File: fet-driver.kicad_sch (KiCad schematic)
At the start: 32 parts, among them Q21 AO3401, Q22 AO3401, Q23 AO3401, Q24 AO3401, Q25 AO3401, Q26 AO3401, Q27 AO3401, Q28 AO3401

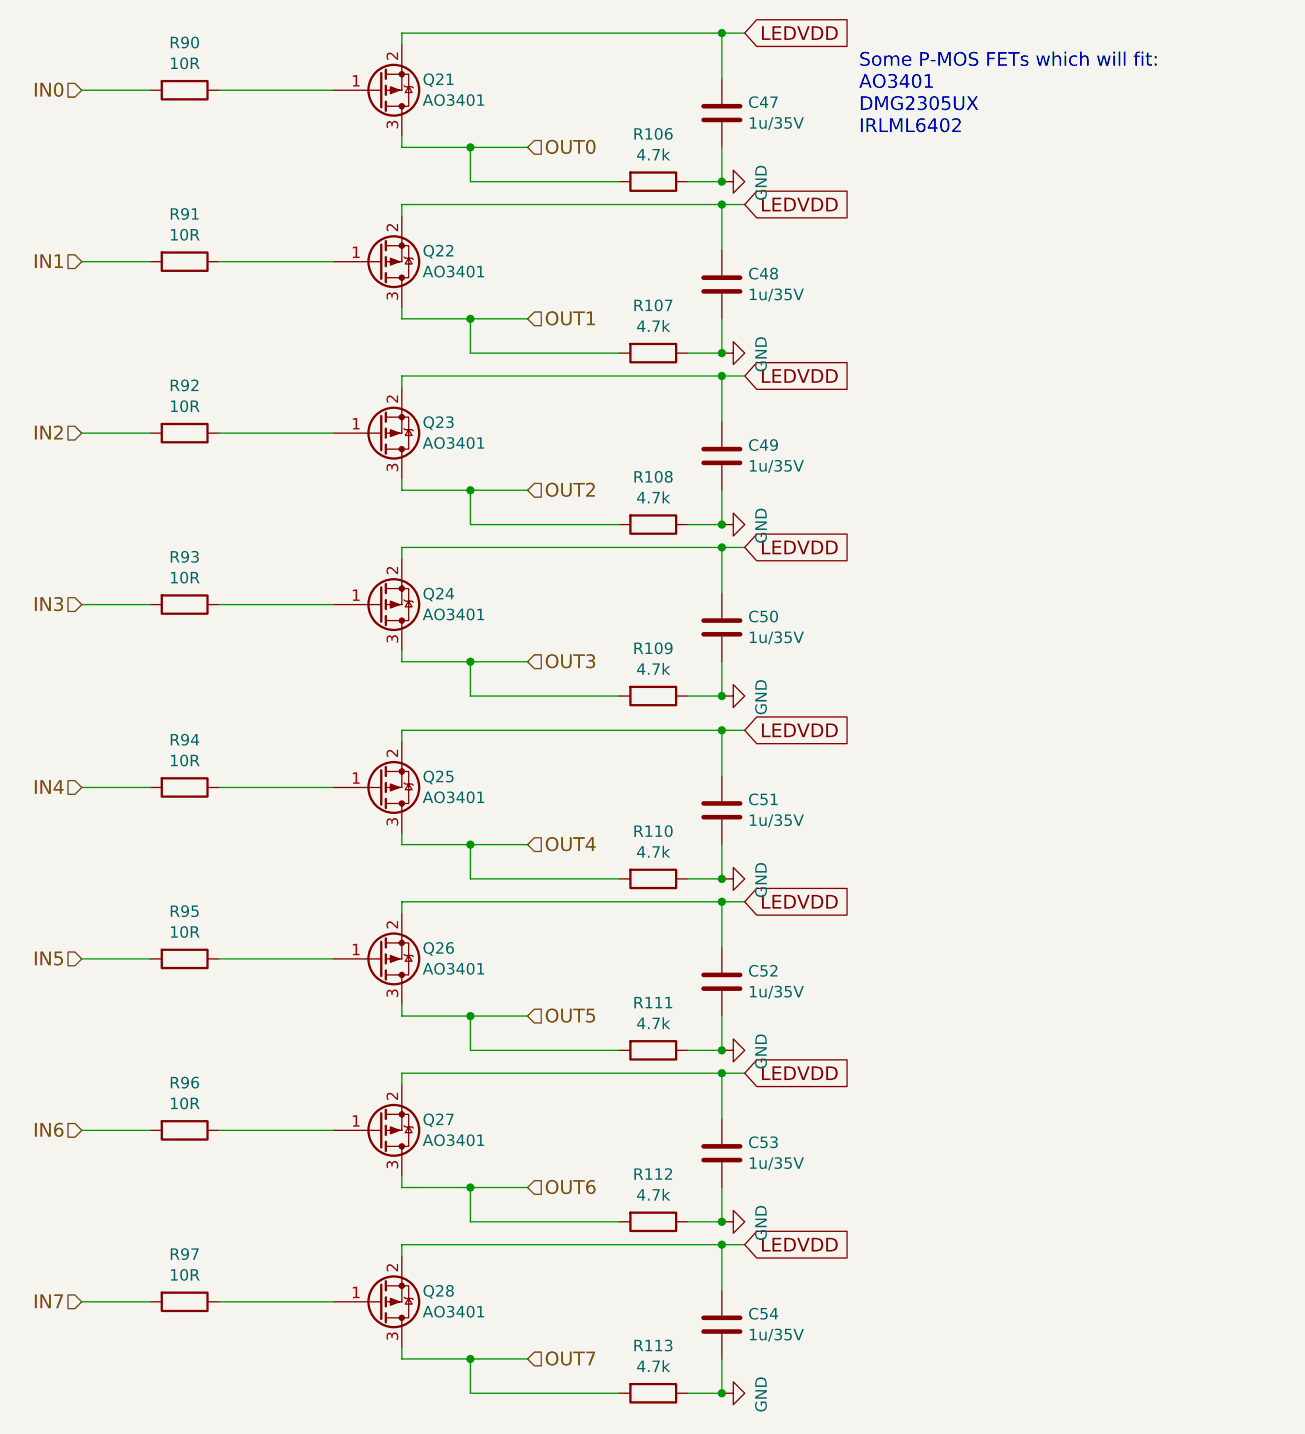
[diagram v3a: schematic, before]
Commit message: WROOM32 coupling capacitor order fixed; Added FB on long line to board left-most sensors
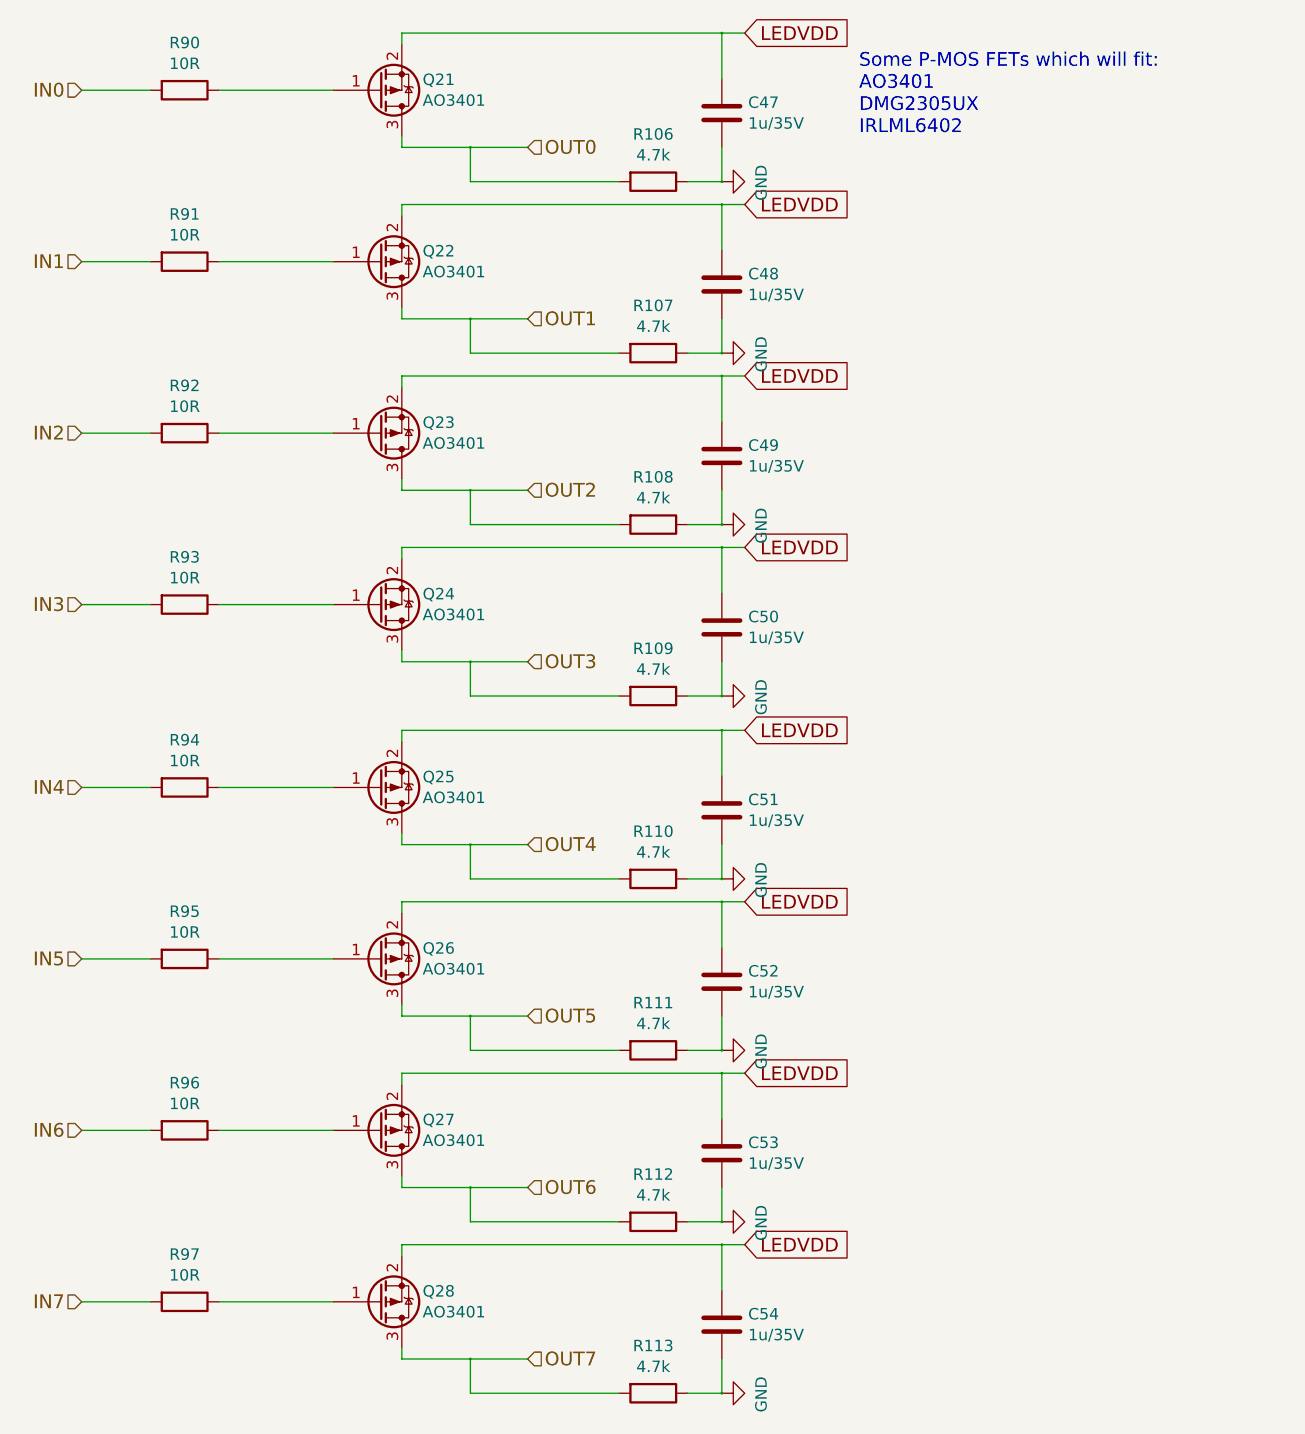
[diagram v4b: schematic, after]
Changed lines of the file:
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@@
-(kicad_sch (version 20200618) (host eeschema "5.99.0-unknown-7340c97~89~ubuntu18.04.1")
-  (page 1 10)
+(kicad_sch (version 20200714) (host eeschema "5.99.0-unknown-e5f2015a9~89~ubuntu18.04.1")
+  (page 0 10)
   (paper "A4")
-  (junction (at 119.38 39.37) (diameter 0) (color 0 0 0 0))
-  (junction (at 119.38 58.42) (diameter 0) (color 0 0 0 0))
-  (junction (at 119.38 77.47) (diameter 0) (color 0 0 0 0))
-  (junction (at 119.38 96.52) (diameter 0) (color 0 0 0 0))
-  (junction (at 119.38 116.84) (diameter 0) (color 0 0 0 0))
-  (junction (at 119.38 135.89) (diameter 0) (color 0 0 0 0))
-  (junction (at 119.38 154.94) (diameter 0) (color 0 0 0 0))
-  (junction (at 119.38 173.99) (diameter 0) (color 0 0 0 0))
-  (junction (at 147.32 26.67) (diameter 0) (color 0 0 0 0))
-  (junction (at 147.32 43.18) (diameter 0) (color 0 0 0 0))
-  (junction (at 147.32 45.72) (diameter 0) (color 0 0 0 0))
-  (junction (at 147.32 62.23) (diameter 0) (color 0 0 0 0))
-  (junction (at 147.32 64.77) (diameter 0) (color 0 0 0 0))
-  (junction (at 147.32 81.28) (diameter 0) (color 0 0 0 0))
-  (junction (at 147.32 83.82) (diameter 0) (color 0 0 0 0))
-  (junction (at 147.32 100.33) (diameter 0) (color 0 0 0 0))
-  (junction (at 147.32 104.14) (diameter 0) (color 0 0 0 0))
-  (junction (at 147.32 120.65) (diameter 0) (color 0 0 0 0))
-  (junction (at 147.32 123.19) (diameter 0) (color 0 0 0 0))
-  (junction (at 147.32 139.7) (diameter 0) (color 0 0 0 0))
-  (junction (at 147.32 142.24) (diameter 0) (color 0 0 0 0))
-  (junction (at 147.32 158.75) (diameter 0) (color 0 0 0 0))
-  (junction (at 147.32 161.29) (diameter 0) (color 0 0 0 0))
-  (junction (at 147.32 177.8) (diameter 0) (color 0 0 0 0))
+  (junction (at 119.38 39.37) (diameter 0.3048) (color 0 0 0 0))
+  (junction (at 119.38 58.42) (diameter 0.3048) (color 0 0 0 0))
+  (junction (at 119.38 77.47) (diameter 0.3048) (color 0 0 0 0))
+  (junction (at 119.38 96.52) (diameter 0.3048) (color 0 0 0 0))
+  (junction (at 119.38 116.84) (diameter 0.3048) (color 0 0 0 0))
+  (junction (at 119.38 135.89) (diameter 0.3048) (color 0 0 0 0))
+  (junction (at 119.38 154.94) (diameter 0.3048) (color 0 0 0 0))
+  (junction (at 119.38 173.99) (diameter 0.3048) (color 0 0 0 0))
+  (junction (at 147.32 26.67) (diameter 0.3048) (color 0 0 0 0))
+  (junction (at 147.32 43.18) (diameter 0.3048) (color 0 0 0 0))
+  (junction (at 147.32 45.72) (diameter 0.3048) (color 0 0 0 0))
+  (junction (at 147.32 62.23) (diameter 0.3048) (color 0 0 0 0))
+  (junction (at 147.32 64.77) (diameter 0.3048) (color 0 0 0 0))
+  (junction (at 147.32 81.28) (diameter 0.3048) (color 0 0 0 0))
+  (junction (at 147.32 83.82) (diameter 0.3048) (color 0 0 0 0))
+  (junction (at 147.32 100.33) (diameter 0.3048) (color 0 0 0 0))
+  (junction (at 147.32 104.14) (diameter 0.3048) (color 0 0 0 0))
+  (junction (at 147.32 120.65) (diameter 0.3048) (color 0 0 0 0))
+  (junction (at 147.32 123.19) (diameter 0.3048) (color 0 0 0 0))
+  (junction (at 147.32 139.7) (diameter 0.3048) (color 0 0 0 0))
+  (junction (at 147.32 142.24) (diameter 0.3048) (color 0 0 0 0))
+  (junction (at 147.32 158.75) (diameter 0.3048) (color 0 0 0 0))
+  (junction (at 147.32 161.29) (diameter 0.3048) (color 0 0 0 0))
+  (junction (at 147.32 177.8) (diameter 0.3048) (color 0 0 0 0))
   (wire (pts (xy 76.2 33.02) (xy 83.82 33.02))
     (stroke (width 0) (type solid) (color 0 0 0 0))
